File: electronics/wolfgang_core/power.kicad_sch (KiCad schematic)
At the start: 95 parts, among them IC1 LM5157RTER, J1 Power Supply, J2 Battery, Q1 SUM110P06-08L-E3, Q2 SUM110P06-08L-E3, Q3 SUM110P06-08L-E3, Q4 SUM110P06-08L-E3, Q5 BSS138P,215, Q6 SUM110P06-08L-E3, SW1 power_switch, U10 LM5001MA, U11 ACS724LLCTR-50AB, U12 SN74AHCT1G08, U7 ROF-78E3.3-0.5SMD-R, U8 ROF-78E5.0-0.5SMD-R, U9 LTC4418IUF-PBF

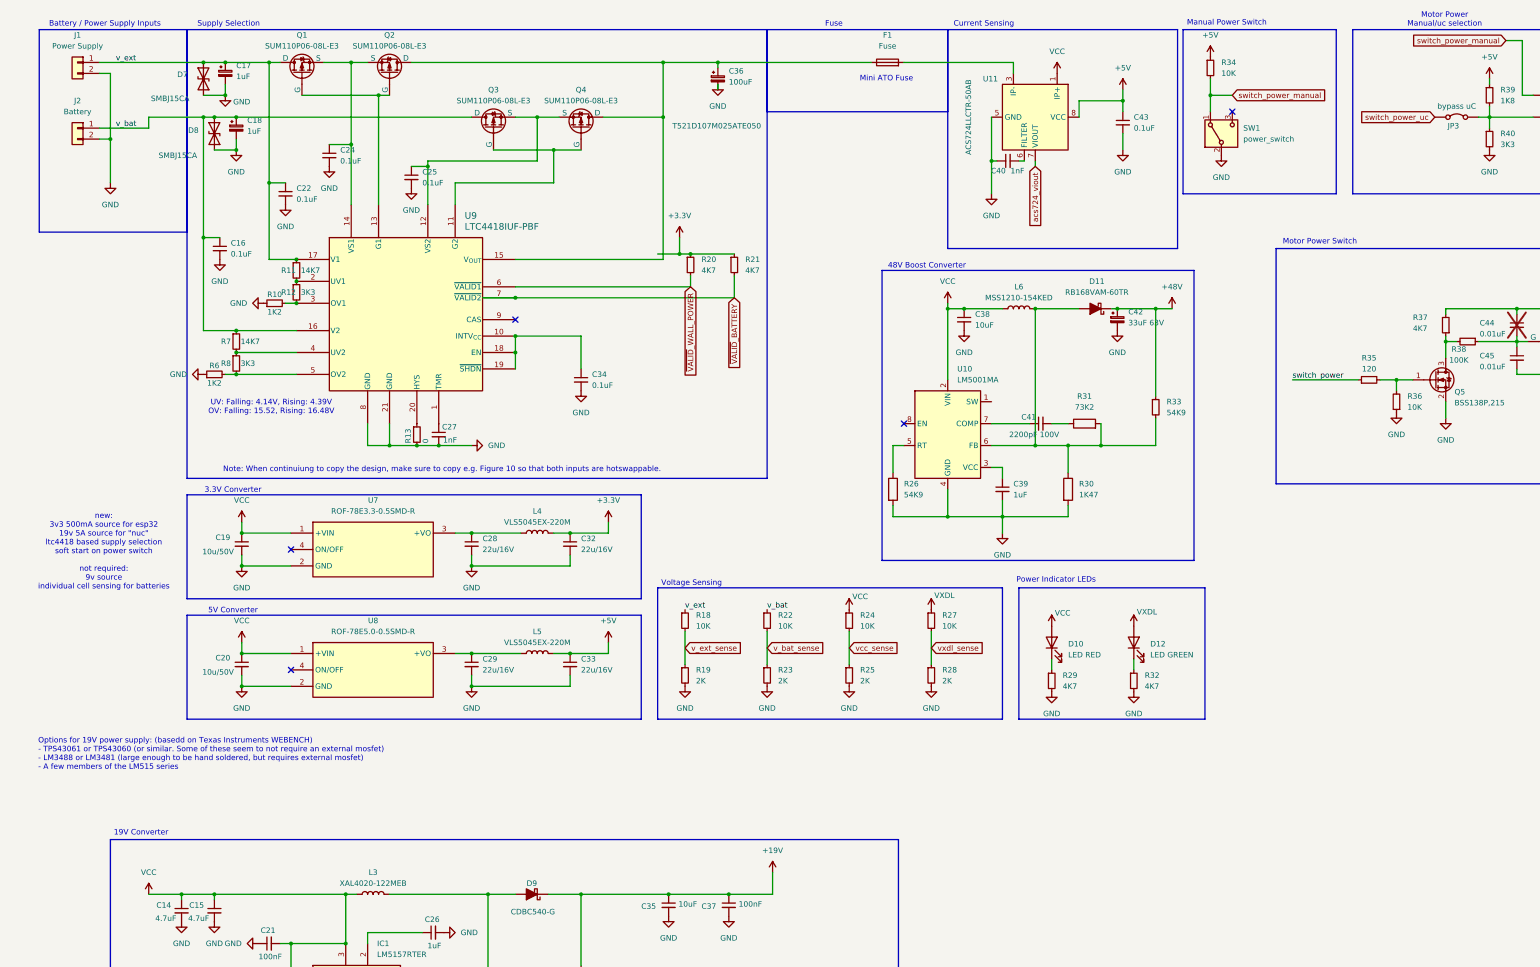
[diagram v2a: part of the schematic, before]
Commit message: Assign almost all Footprints
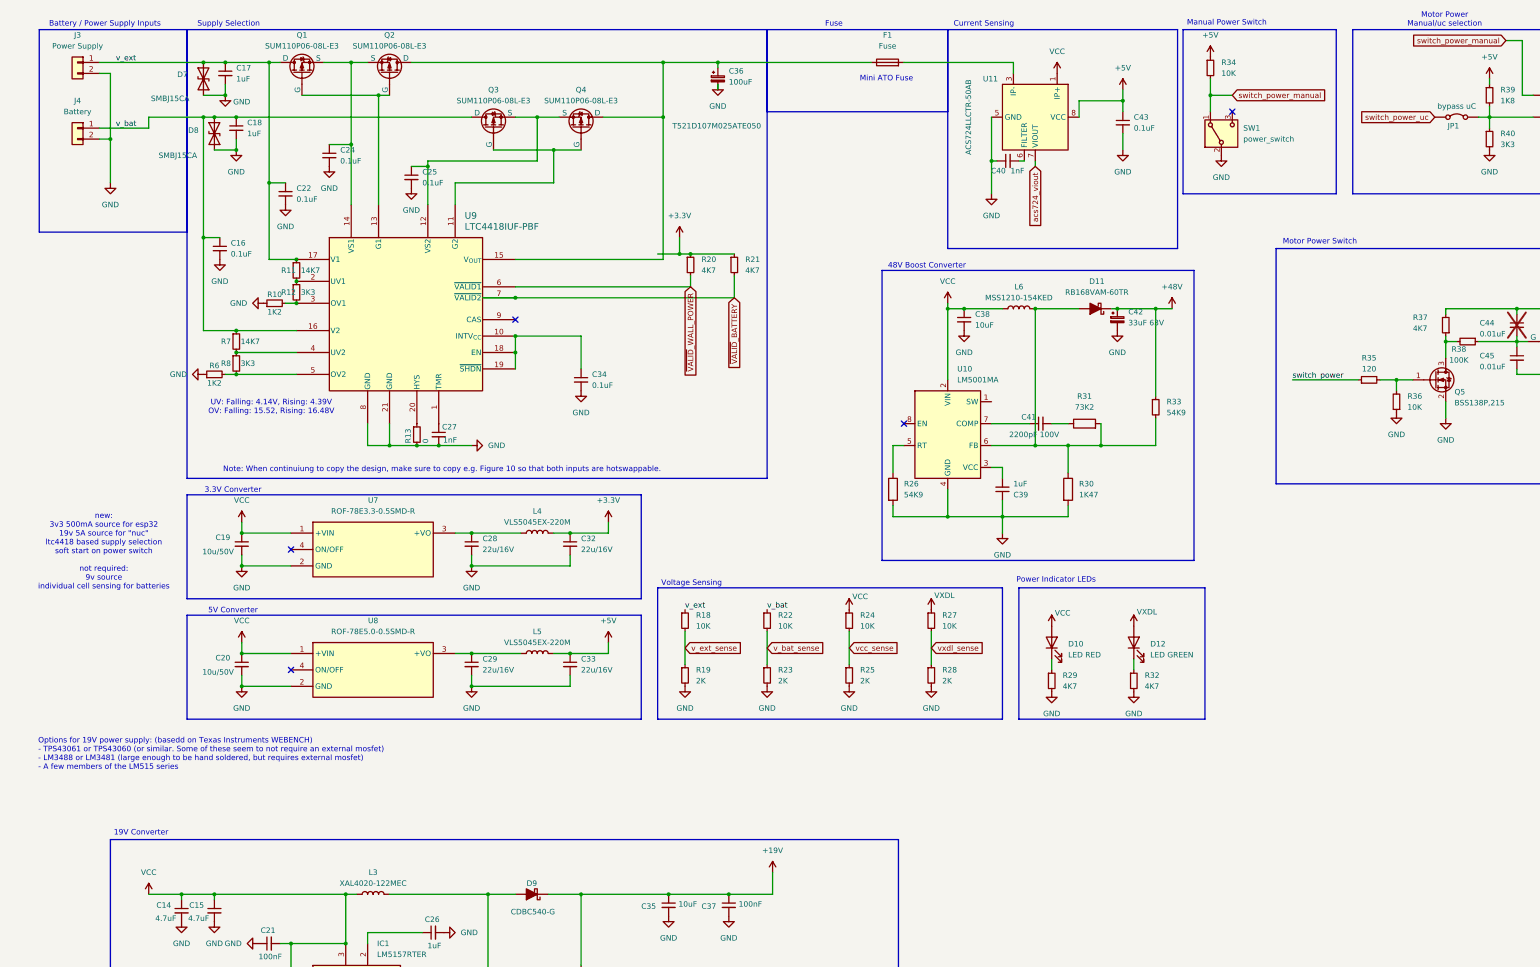
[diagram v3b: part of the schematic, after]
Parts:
- removed C17, C18: 1uF, symbol Device:C_Polarized_Small
- added C17, C18: 1uF, Capacitor_SMD:C_0805_2012Metric, symbol Device:C_Small
- C14, C15, C16, C21, C22, C23, C24, C25, C26, C27, C30, C31, C34, C37, C39, C40, C41, C43, C44, C45: footprint (none) -> Capacitor_SMD:C_0805_2012Metric
- C19, C20, C28, C29, C32, C33, C35, C38, C42: footprint (none) -> Capacitor_SMD:C_1206_3216Metric
- D11: footprint (none) -> Diode_SMD:D_TUMD2
- D9: footprint (none) -> Diode_SMD:D_SMC
- JP1: renamed from JP3; footprint (none) -> Connector_PinHeader_2.54mm:PinHeader_1x02_P2.54mm_Vertical
- L3: value XAL4020-122MEB -> XAL4020-122MEC; footprint (none) -> Inductor_SMD:L_Coilcraft_XAL4020-XXX
- L4, L5: footprint (none) -> bitbots:VLS5045EX330M
- L6: footprint (none) -> Inductor_SMD:L_Coilcraft_MSS1210-XXX
- R10, R11, R12, R13, R14, R15, R16, R17, R18, R19, R20, R21, R22, R23, R24, R25, R26, R27, R28, R29, R30, R31, R32, R33, R34, R35, R36, R37, R38, R39, R40, R6, R7, R8, R9: footprint (none) -> Resistor_SMD:R_0805_2012Metric
- SW1: footprint (none) -> Connector_Molex:Molex_SPOX_5267-04A_1x04_P2.50mm_Vertical
- renumbered J1 to J3, J2 to J4
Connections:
- net GND: now also C39.1, C17.2, C18.2; no longer C39.2
- net v_bat: now also C18.1
- net v_ext: now also C17.1
- net at U10.3 (VCC): now also C39.2; no longer C39.1
